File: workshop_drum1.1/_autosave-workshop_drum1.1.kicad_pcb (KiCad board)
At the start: 2 copper layers, 41 parts, among them J1 9v_Battery_Clip, J2 Trigger_Input, J3 Output, U1 LM358, U2 7414, U3 78L05

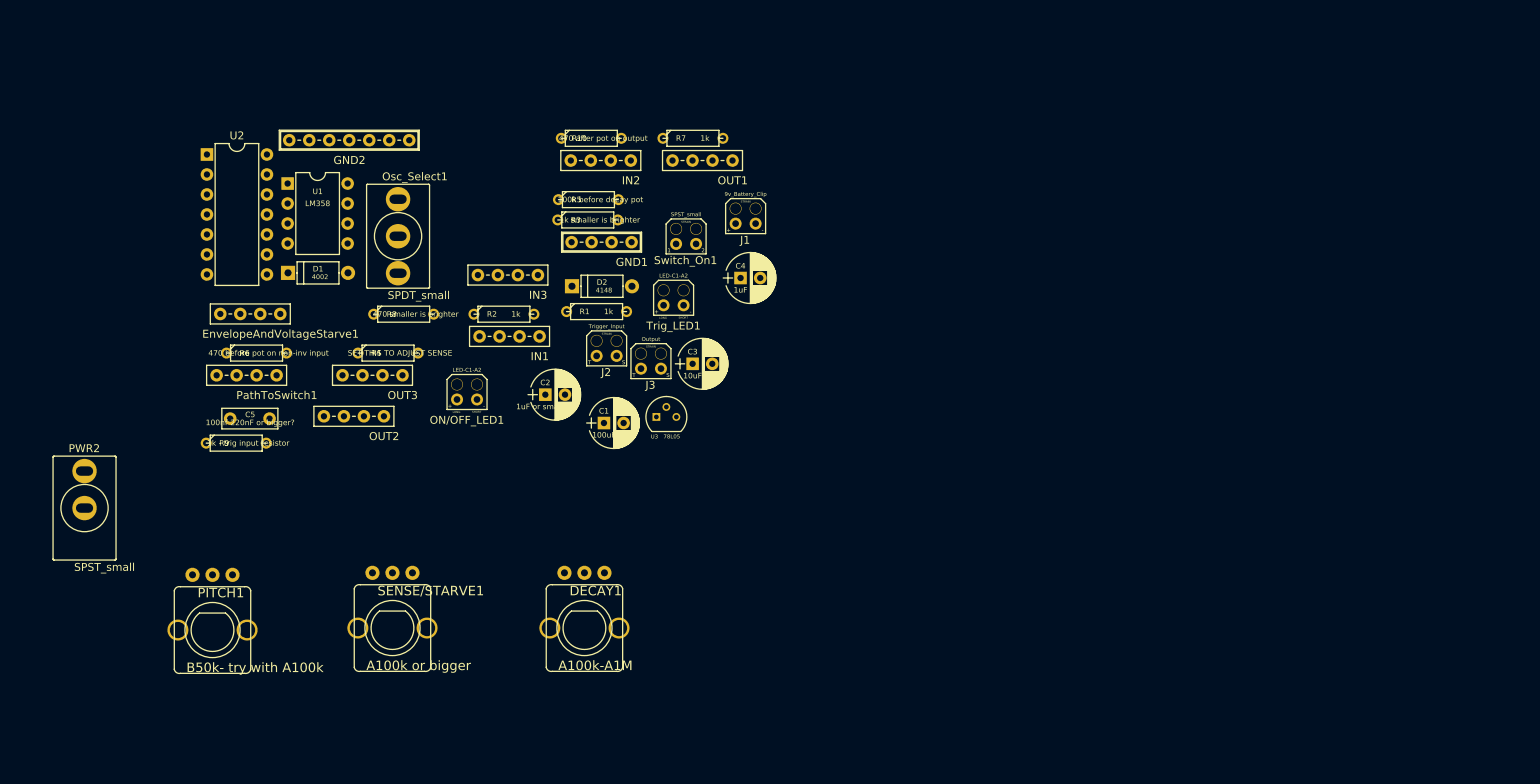
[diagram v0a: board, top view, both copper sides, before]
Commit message: P1.1 started working on breadboard strip
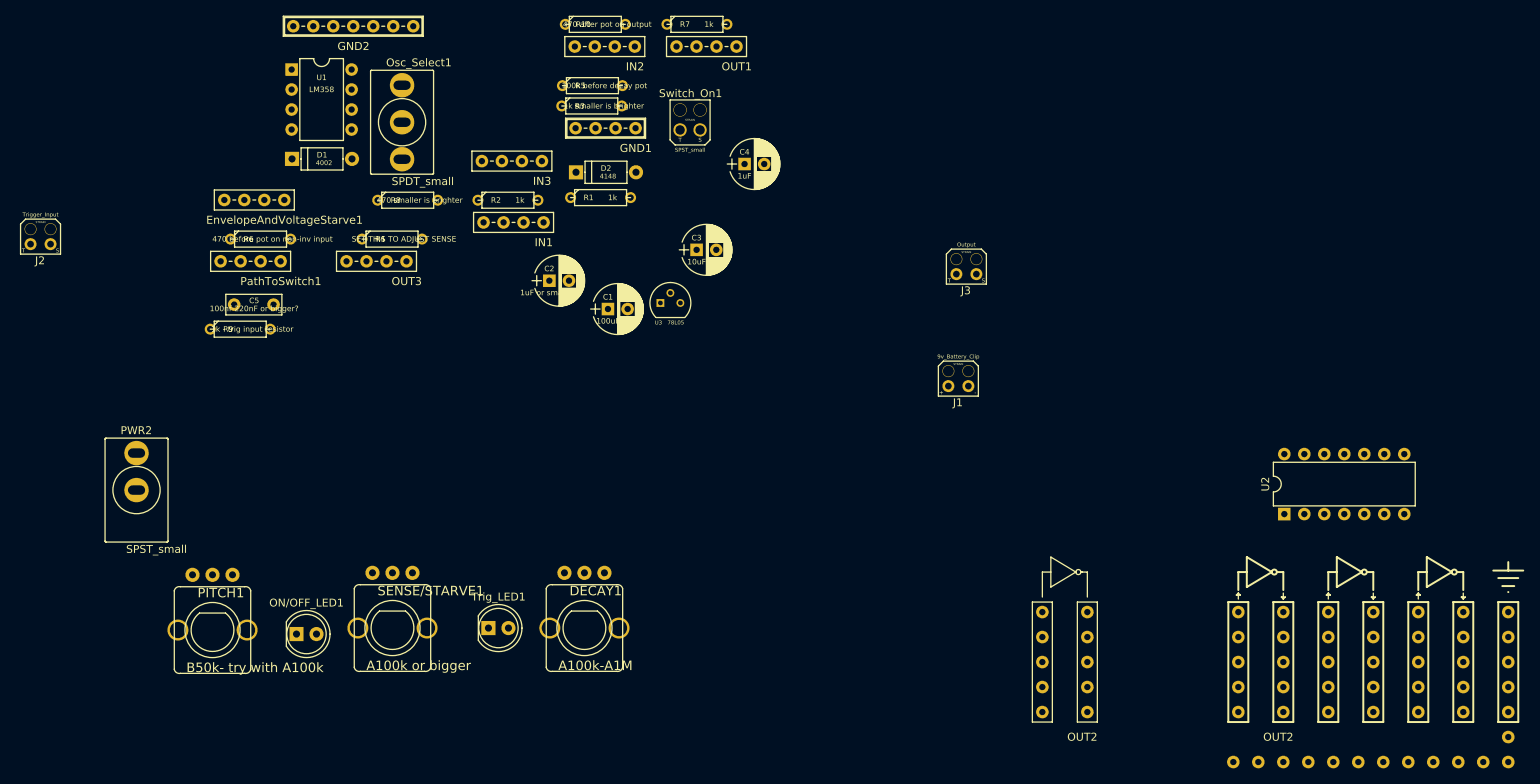
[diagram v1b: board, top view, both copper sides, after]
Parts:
- added OUT2: BreadBoardStrip, zfoot:BREAKOUT, F.Cu at (213.4, 99.6)
- ON/OFF_LED1, Trig_LED1: footprint zfoot:LED_wired -> zfoot:LED_D5.0mm
- OUT2: footprint zfoot:BreadBoardStrip_4 -> zfoot:BREAKOUT
- Switch_On1: footprint zfoot:SPST_Wired -> zfoot:Jack_Instrument_Bigger
- moved U2 144.3 mm to (219.2, 80.8), turned to 90 degrees
- moved OUT2 92.9 mm to (188.5, 99.6)
- moved J2 73.3 mm to (61.2, 46.5)
- moved Trig_LED1 47.3 mm to (118.1, 95.2)
- moved J3 41.8 mm to (178.8, 50.3)
- moved ON/OFF_LED1 36.8 mm to (93.7, 96.0)
- moved J1 34.0 mm to (177.8, 64.5)
- moved GND2 14.5 mm to (100.9, 18.8)
- moved C2 14.5 mm to (125.8, 51.1)
- moved C3 14.5 mm to (144.5, 47.2)
- moved C4 14.5 mm to (150.6, 36.3)
- moved D1 14.5 mm to (93.2, 35.7)
- moved D2 14.5 mm to (129.2, 37.4)
- moved IN1 14.5 mm to (121.3, 43.7)
- moved IN2 14.5 mm to (132.9, 21.4)
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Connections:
- OUT2 pad 1: Net-(OUT2-Pad1) -> (no net)
